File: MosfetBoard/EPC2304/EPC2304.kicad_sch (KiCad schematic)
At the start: 2 parts, among them J14 BATT-Conn2, J9 BATT-Conn1

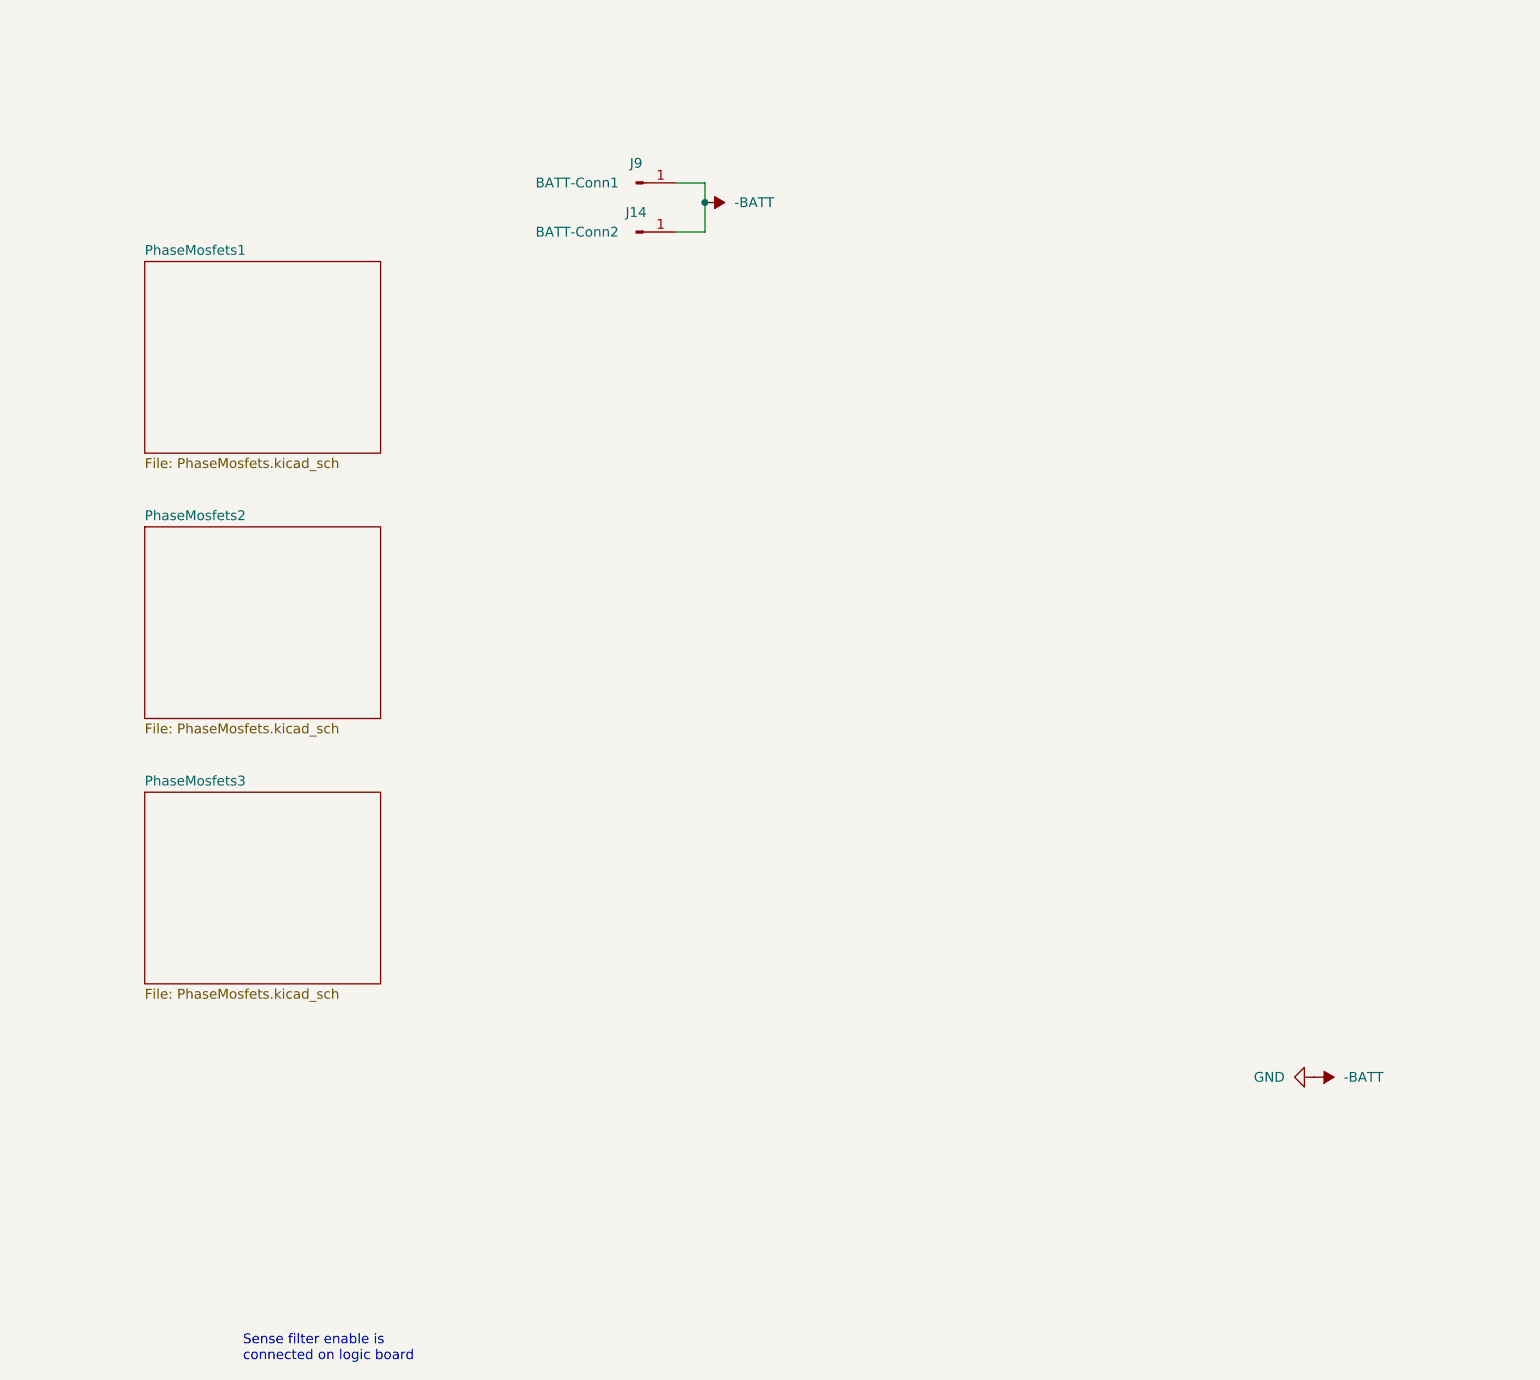
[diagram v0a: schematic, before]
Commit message: v2.8.0 - Small Hall sensors
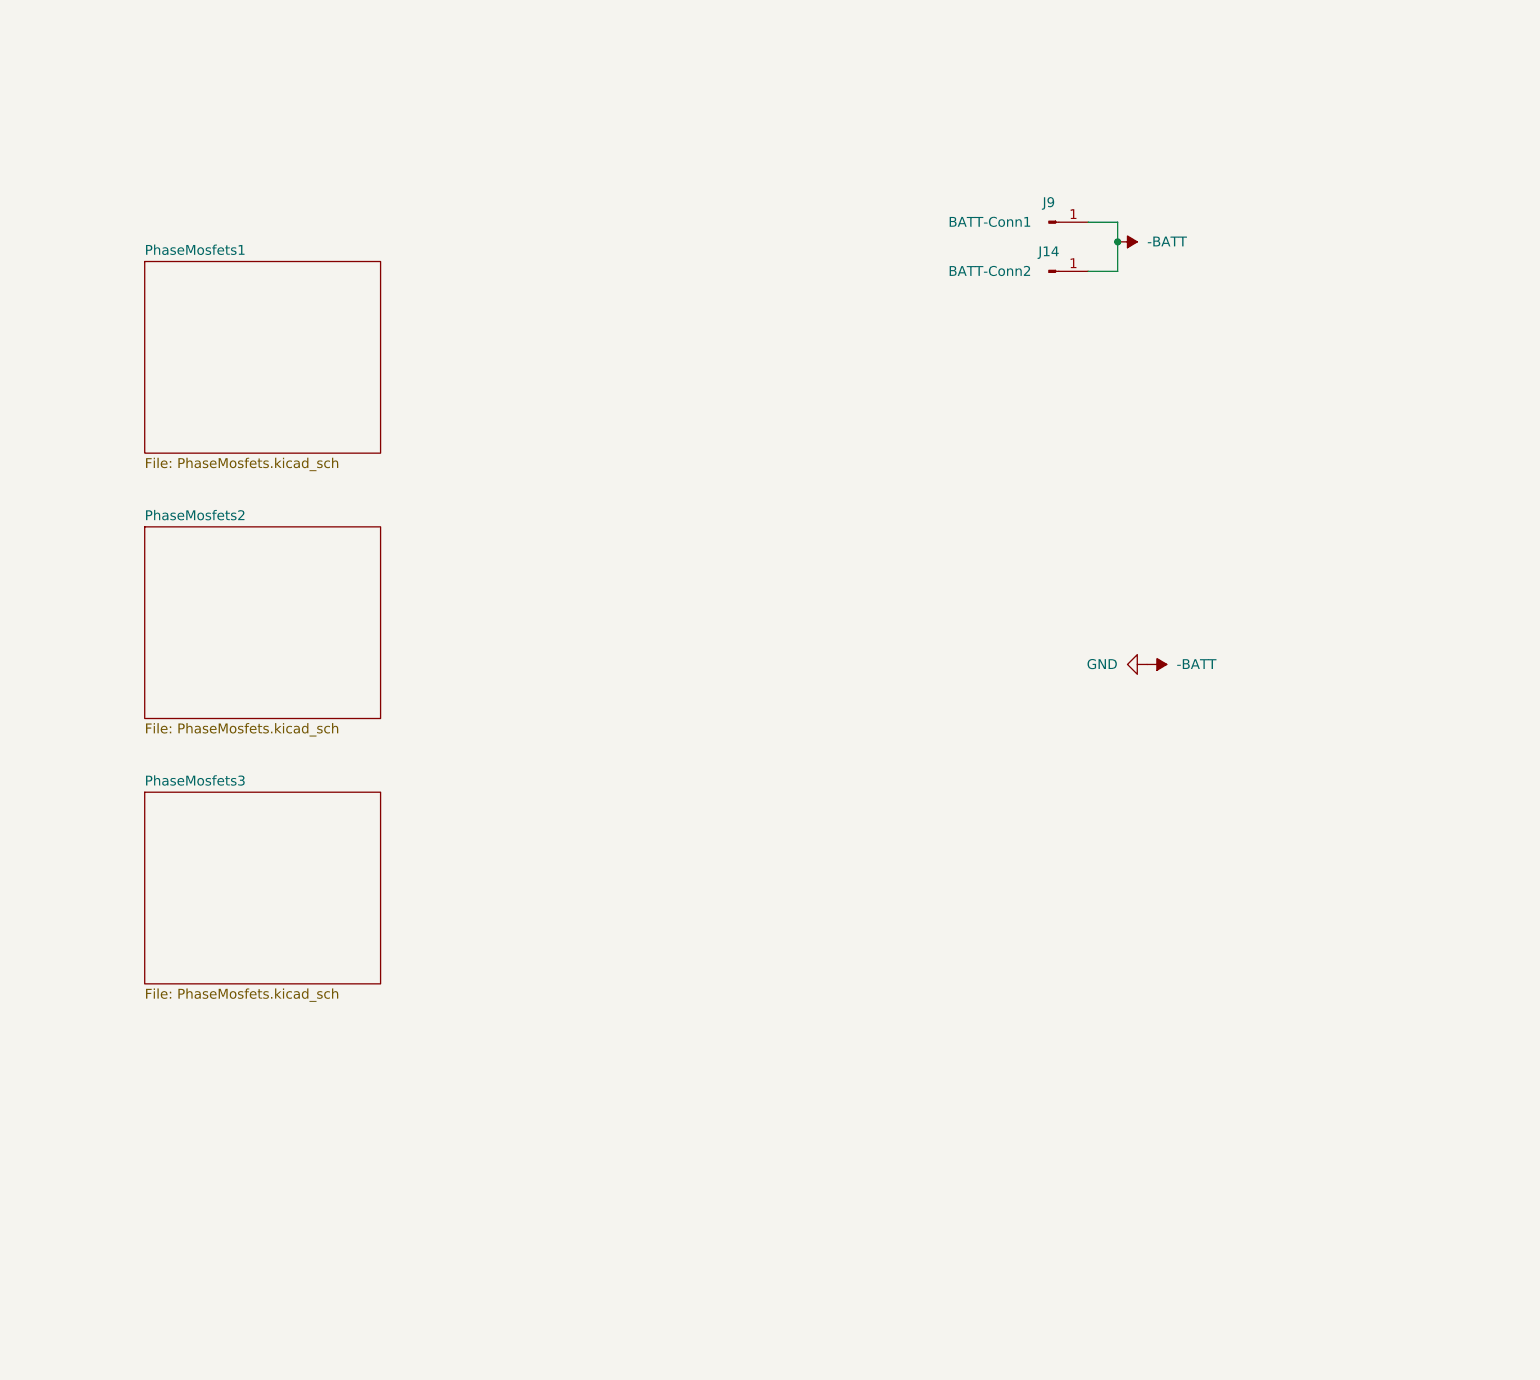
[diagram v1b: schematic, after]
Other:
- note removed: "Sense filter enable is connected on logic board"
- moved on the sheet: J14, J9
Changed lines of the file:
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@@
 (kicad_sch (version 20230121) (generator eeschema)
   (paper "A4")
-  (junction (at 110.49 43.18) (diameter 0) (color 0 0 0 0)
+  (junction (at 163.83 48.26) (diameter 0) (color 0 0 0 0)
   )
-  (wire (pts (xy 106.68 46.99) (xy 110.49 46.99))
+  (wire (pts (xy 160.02 52.07) (xy 163.83 52.07))
     (stroke (width 0) (type default))
   )
-  (wire (pts (xy 106.68 40.64) (xy 110.49 40.64))
+  (wire (pts (xy 160.02 45.72) (xy 163.83 45.72))
     (stroke (width 0) (type default))
   )
-  (wire (pts (xy 110.49 40.64) (xy 110.49 43.18))
+  (wire (pts (xy 163.83 45.72) (xy 163.83 48.26))
     (stroke (width 0) (type default))
   )
-  (wire (pts (xy 110.49 46.99) (xy 110.49 43.18))
+  (wire (pts (xy 163.83 52.07) (xy 163.83 48.26))
     (stroke (width 0) (type default))
   )
-  (text "Sense filter enable is \nconnected on logic board" (at 50.8 193.04 0)
-    (effects (font (size 1.27 1.27)) (justify left bottom))
-  )
-  (symbol (lib_id "power:-BATT") (at 110.49 43.18 270) (unit 1)
+  (symbol (lib_id "power:-BATT") (at 163.83 48.26 270) (unit 1)
     (in_bom yes) (on_board yes) (dnp no) (fields_autoplaced)
-    (property "Reference" "#PWR02" (at 106.68 43.18 0)
+    (property "Reference" "#PWR02" (at 160.02 48.26 0)
       (effects (font (size 1.27 1.27)) hide)
     )
-    (property "Value" "-BATT" (at 114.3 43.18 90)
+    (property "Value" "-BATT" (at 167.64 48.26 90)
       (effects (font (size 1.27 1.27)) (justify left))
     )
-    (property "Footprint" "" (at 110.49 43.18 0)
+    (property "Footprint" "" (at 163.83 48.26 0)
       (effects (font (size 1.27 1.27)) hide)
     )
-    (property "Datasheet" "" (at 110.49 43.18 0)
+    (property "Datasheet" "" (at 163.83 48.26 0)
       (effects (font (size 1.27 1.27)) hide)
     )
@@
     )
   )
-  (symbol (lib_id "Connector:Conn_01x01_Pin") (at 101.6 46.99 0) (unit 1)
+  (symbol (lib_id "Connector:Conn_01x01_Pin") (at 154.94 52.07 0) (unit 1)
     (in_bom yes) (on_board yes) (dnp no)
-    (property "Reference" "J14" (at 101.6 44.45 0)
+    (property "Reference" "J14" (at 154.94 49.53 0)
       (effects (font (size 1.27 1.27)))
     )
-    (property "Value" "BATT-Conn2" (at 93.98 46.99 0)
+    (property "Value" "BATT-Conn2" (at 147.32 52.07 0)
       (effects (font (size 1.27 1.27)))
     )
-    (property "Footprint" "Connector_Wire:SolderWirePad_1x01_SMD_5x10mm" (at 101.6 46.99 0)
+    (property "Footprint" "Connector_Wire:SolderWirePad_1x01_SMD_5x10mm" (at 154.94 52.07 0)
       (effects (font (size 1.27 1.27)) hide)
     )
-    (property "Datasheet" "~" (at 101.6 46.99 0)
+    (property "Datasheet" "~" (at 154.94 52.07 0)
       (effects (font (size 1.27 1.27)) hide)
     )
@@
     )
   )
-  (symbol (lib_id "Connector:Conn_01x01_Pin") (at 101.6 40.64 0) (unit 1)
+  (symbol (lib_id "Connector:Conn_01x01_Pin") (at 154.94 45.72 0) (unit 1)
     (in_bom yes) (on_board yes) (dnp no)
-    (property "Reference" "J9" (at 101.6 38.1 0)
+    (property "Reference" "J9" (at 154.94 43.18 0)
       (effects (font (size 1.27 1.27)))
     )
-    (property "Value" "BATT-Conn1" (at 93.98 40.64 0)
+    (property "Value" "BATT-Conn1" (at 147.32 45.72 0)
       (effects (font (size 1.27 1.27)))
     )
-    (property "Footprint" "Connector_Wire:SolderWirePad_1x01_SMD_5x10mm" (at 101.6 40.64 0)
+    (property "Footprint" "Connector_Wire:SolderWirePad_1x01_SMD_5x10mm" (at 154.94 45.72 0)
       (effects (font (size 1.27 1.27)) hide)
     )
-    (property "Datasheet" "~" (at 101.6 40.64 0)
+    (property "Datasheet" "~" (at 154.94 45.72 0)
       (effects (font (size 1.27 1.27)) hide)
     )
@@
     )
   )
-  (symbol (lib_id "power:-BATT") (at 189.23 156.21 270) (unit 1)
+  (symbol (lib_id "power:-BATT") (at 167.64 102.87 270) (unit 1)
     (in_bom yes) (on_board yes) (dnp no) (fields_autoplaced)
-    (property "Reference" "#PWR023" (at 185.42 156.21 0)
+    (property "Reference" "#PWR023" (at 163.83 102.87 0)
       (effects (font (size 1.27 1.27)) hide)
     )
-    (property "Value" "-BATT" (at 193.04 156.21 90)
+    (property "Value" "-BATT" (at 171.45 102.87 90)
       (effects (font (size 1.27 1.27)) (justify left))
     )
-    (property "Footprint" "" (at 189.23 156.21 0)
+    (property "Footprint" "" (at 167.64 102.87 0)
       (effects (font (size 1.27 1.27)) hide)
     )
-    (property "Datasheet" "" (at 189.23 156.21 0)
+    (property "Datasheet" "" (at 167.64 102.87 0)
       (effects (font (size 1.27 1.27)) hide)
     )
@@
     )
   )
-  (symbol (lib_id "power:GND") (at 189.23 156.21 270) (unit 1)
+  (symbol (lib_id "power:GND") (at 167.64 102.87 270) (unit 1)
     (in_bom yes) (on_board yes) (dnp no) (fields_autoplaced)
-    (property "Reference" "#PWR024" (at 182.88 156.21 0)
+    (property "Reference" "#PWR024" (at 161.29 102.87 0)
       (effects (font (size 1.27 1.27)) hide)
     )
-    (property "Value" "GND" (at 185.42 156.21 90)
+    (property "Value" "GND" (at 163.83 102.87 90)
       (effects (font (size 1.27 1.27)) (justify right))
     )
-    (property "Footprint" "" (at 189.23 156.21 0)
+    (property "Footprint" "" (at 167.64 102.87 0)
       (effects (font (size 1.27 1.27)) hide)
     )
-    (property "Datasheet" "" (at 189.23 156.21 0)
+    (property "Datasheet" "" (at 167.64 102.87 0)
       (effects (font (size 1.27 1.27)) hide)
     )

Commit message: v3.0.0 - GaN redesign begin
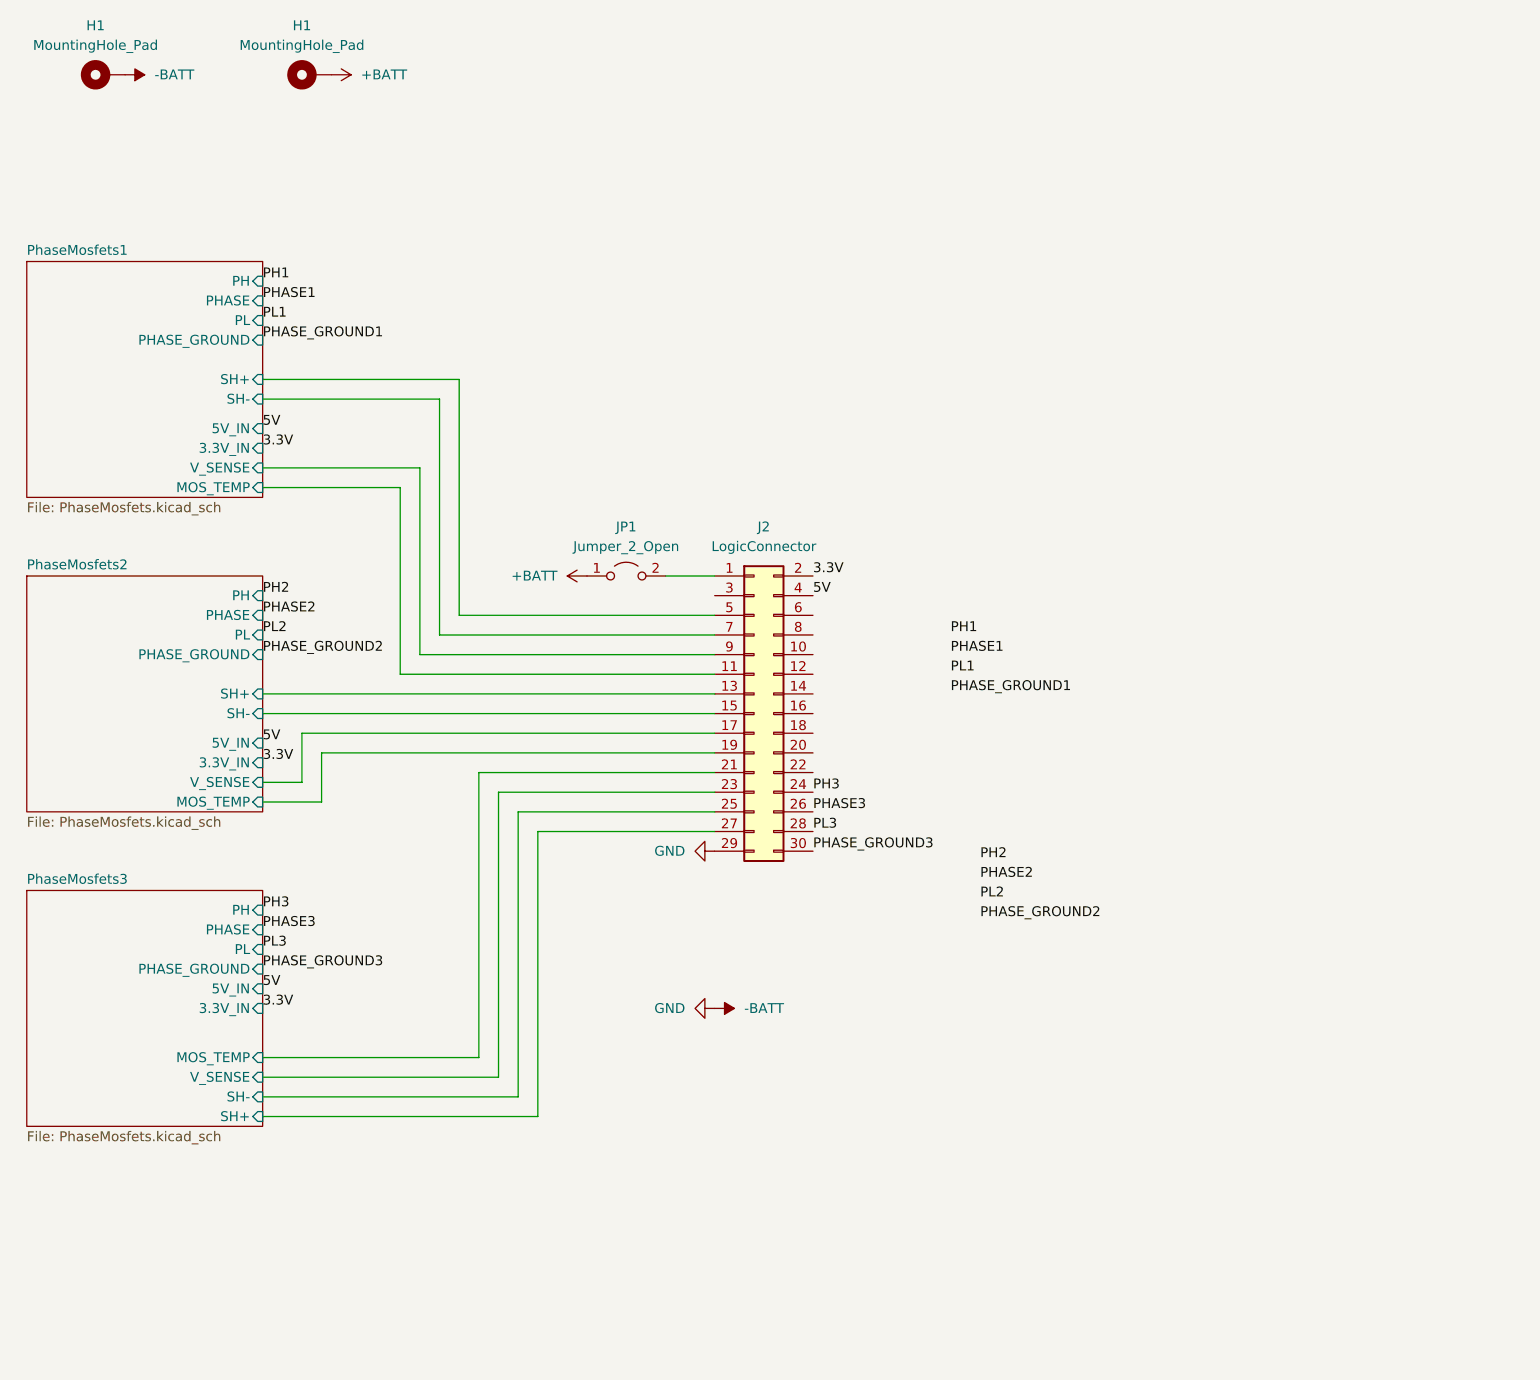
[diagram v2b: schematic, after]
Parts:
- removed J14: BATT-Conn2, Connector_Wire:SolderWirePad_1x01_SMD_5x10mm, symbol Connector:Conn_01x01_Pin
- removed J9: BATT-Conn1, Connector_Wire:SolderWirePad_1x01_SMD_5x10mm, symbol Connector:Conn_01x01_Pin
- added H1 (x2): MountingHole_Pad, MountingHole:MountingHole_5.3mm_M5_Pad_Via, symbol Mechanical:MountingHole_Pad
- added J2: LogicConnector, Connector_PinSocket_2.54mm:PinSocket_2x15_P2.54mm_Vertical, symbol Connector_Generic:Conn_02x15_Odd_Even
- added JP1: Jumper_2_Open, symbol Jumper:Jumper_2_Open
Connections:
- net -BATT: now also H1.1, J2.29 (Pin_29)
- new net: J2.1 (Pin_1), JP1.2 (B)
- new net +BATT: H1.1, JP1.1 (A)
- new net 3.3V: J2.2 (Pin_2)
- new net 5V: J2.4 (Pin_4)
- new net PH3: J2.24 (Pin_24)
- new net PHASE3: J2.26 (Pin_26)
- new net PHASE_GROUND3: J2.30 (Pin_30)
- new net PL3: J2.28 (Pin_28)
- new net PhaseMosfets1/MOS_TEMP: J2.11 (Pin_11)
- new net PhaseMosfets1/SH+: J2.5 (Pin_5)
- new net PhaseMosfets1/SH-: J2.7 (Pin_7)
- new net PhaseMosfets1/V_SENSE: J2.9 (Pin_9)
- new net PhaseMosfets2/MOS_TEMP: J2.19 (Pin_19)
- new net PhaseMosfets2/SH+: J2.13 (Pin_13)
- new net PhaseMosfets2/SH-: J2.15 (Pin_15)
- new net PhaseMosfets2/V_SENSE: J2.17 (Pin_17)
- new net PhaseMosfets3/MOS_TEMP: J2.21 (Pin_21)
- new net PhaseMosfets3/SH+: J2.27 (Pin_27)
- new net PhaseMosfets3/SH-: J2.25 (Pin_25)
- new net PhaseMosfets3/V_SENSE: J2.23 (Pin_23)
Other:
- sheet PhaseMosfets1 ports: added 3.3V_IN, 5V_IN, MOS_TEMP, PH, PHASE, PHASE_GROUND, PL, SH+, SH-, V_SENSE; removed none
- sheet PhaseMosfets2 ports: added 3.3V_IN, 5V_IN, MOS_TEMP, PH, PHASE, PHASE_GROUND, PL, SH+, SH-, V_SENSE; removed none
- sheet PhaseMosfets3 ports: added 3.3V_IN, 5V_IN, MOS_TEMP, PH, PHASE, PHASE_GROUND, PL, SH+, SH-, V_SENSE; removed none
